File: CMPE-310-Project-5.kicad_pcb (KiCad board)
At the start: 4 copper layers, 10 parts, among them J1 DSUB-9, U1 max235cpg, U2 8255, U3 pkd8279, U4 8086_Min_Mode, U5 8255, U6 8255

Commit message: File Updates (RAM wired)
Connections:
- Bank0 pad 10: unconnected-(Bank0-Pad10) -> /CMOS_wires/A3
- Bank0 pad 11: unconnected-(Bank0-Pad11) -> /CMOS_wires/A2
- Bank0 pad 12: unconnected-(Bank0-Pad12) -> /CMOS_wires/A1
- Bank0 pad 2: unconnected-(Bank0-Pad2) -> /CMOS_wires/A17
- Bank0 pad 22: unconnected-(Bank0-Pad22) -> /CMOS_wires/CS1
- Bank0 pad 23: unconnected-(Bank0-Pad23) -> /CMOS_wires/A11
- Bank0 pad 24: unconnected-(Bank0-Pad24) -> /RD
- Bank0 pad 25: unconnected-(Bank0-Pad25) -> /CMOS_wires/A12
- Bank0 pad 26: unconnected-(Bank0-Pad26) -> /CMOS_wires/A10
- Bank0 pad 27: unconnected-(Bank0-Pad27) -> /CMOS_wires/A9
- Bank0 pad 28: unconnected-(Bank0-Pad28) -> /CMOS_wires/A14
- Bank0 pad 29: unconnected-(Bank0-Pad29) -> /CMOS_wires/A15
- Bank0 pad 3: unconnected-(Bank0-Pad3) -> /CMOS_wires/A16
- Bank0 pad 31: unconnected-(Bank0-Pad31) -> /WR
- Bank0 pad 4: unconnected-(Bank0-Pad4) -> /CMOS_wires/A13
- Bank0 pad 5: unconnected-(Bank0-Pad5) -> /CMOS_wires/A8
- Bank0 pad 6: unconnected-(Bank0-Pad6) -> /CMOS_wires/A7
- Bank0 pad 7: unconnected-(Bank0-Pad7) -> /CMOS_wires/A6
- Bank0 pad 8: unconnected-(Bank0-Pad8) -> /CMOS_wires/A5
- Bank0 pad 9: unconnected-(Bank0-Pad9) -> /CMOS_wires/A4
- Bank1 pad 10: unconnected-(Bank1-Pad10) -> /CMOS_wires/A3
- Bank1 pad 11: unconnected-(Bank1-Pad11) -> /CMOS_wires/A2
- Bank1 pad 12: unconnected-(Bank1-Pad12) -> /CMOS_wires/A1
- Bank1 pad 2: unconnected-(Bank1-Pad2) -> /CMOS_wires/A17
- Bank1 pad 22: unconnected-(Bank1-Pad22) -> /CMOS_wires/CS1
- Bank1 pad 23: unconnected-(Bank1-Pad23) -> /CMOS_wires/A11
- Bank1 pad 24: unconnected-(Bank1-Pad24) -> /RD
- Bank1 pad 25: unconnected-(Bank1-Pad25) -> /CMOS_wires/A12
- Bank1 pad 26: unconnected-(Bank1-Pad26) -> /CMOS_wires/A9
- Bank1 pad 27: unconnected-(Bank1-Pad27) -> /CMOS_wires/A9
- Bank1 pad 28: unconnected-(Bank1-Pad28) -> /CMOS_wires/A14
- Bank1 pad 29: unconnected-(Bank1-Pad29) -> /CMOS_wires/A15
- Bank1 pad 3: unconnected-(Bank1-Pad3) -> /CMOS_wires/A16
- Bank1 pad 31: unconnected-(Bank1-Pad31) -> /WR
- Bank1 pad 4: unconnected-(Bank1-Pad4) -> /CMOS_wires/A13
- Bank1 pad 5: unconnected-(Bank1-Pad5) -> /CMOS_wires/A8
- Bank1 pad 6: unconnected-(Bank1-Pad6) -> /CMOS_wires/A7
- Bank1 pad 7: unconnected-(Bank1-Pad7) -> /CMOS_wires/A6
- Bank1 pad 8: unconnected-(Bank1-Pad8) -> /CMOS_wires/A5
- Bank1 pad 9: unconnected-(Bank1-Pad9) -> /CMOS_wires/A4

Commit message: Updated PCB
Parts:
- added C1: C, Capacitor_SMD:CP_Elec_3x5.3, F.Cu at (236.0, 243.5)
- added C2: C, Capacitor_SMD:CP_Elec_3x5.3, F.Cu at (226.2, 76.1)
- added D1: DIODE, Diode_SMD:D_0201_0603Metric, F.Cu at (263.3, 209.8)
- added D10: LED, LED_SMD:LED_0201_0603Metric, F.Cu at (-1.19, 106.8)
- added D2: DIODE, Diode_SMD:D_0201_0603Metric, F.Cu at (242.7, 72.1)
- added D3: LED, LED_SMD:LED_0201_0603Metric, F.Cu at (1.49, 108.6)
- added D4: LED, LED_SMD:LED_0201_0603Metric, F.Cu at (-3.87, 106.8)
- added D5: LED, LED_SMD:LED_0201_0603Metric, F.Cu at (-3.87, 108.6)
- added D6: LED, LED_SMD:LED_0201_0603Metric, F.Cu at (-6.55, 106.8)
- added D7: LED, LED_SMD:LED_0201_0603Metric, F.Cu at (-6.55, 108.6)
- added D8: LED, LED_SMD:LED_0201_0603Metric, F.Cu at (1.49, 106.8)
- added D9: LED, LED_SMD:LED_0201_0603Metric, F.Cu at (-1.19, 108.6)
- added J10: Conn_01x04_Male, Connector_Harwin:Harwin_M20-89008xx_1x08_P2.54mm_Horizontal, F.Cu at (315.1, 30.0)
- added J11: Conn_01x03_Male, Connector_Harwin:Harwin_M20-89008xx_1x08_P2.54mm_Horizontal, F.Cu at (304.3, 57.0)
- added J12: Conn_01x03_Male, Connector_Harwin:Harwin_M20-89008xx_1x08_P2.54mm_Horizontal, F.Cu at (330.7, 30.0)
- added J13: Conn_01x02_Male, Connector_Harwin:Harwin_M20-89008xx_1x08_P2.54mm_Horizontal, F.Cu at (285.9, 62.1)
- added J14: DSUB-9, parts:DSUB-9, F.Cu at (249.0, 130.6)
- added J15: Conn_01x03_Male, Connector:FanPinHeader_1x03_P2.54mm_Vertical, F.Cu at (369.2, 49.4)
- added J16: Conn_01x20_Male, Connector:FanPinHeader_1x03_P2.54mm_Vertical, F.Cu at (359.6, 49.4)
- added J17: Conn_01x16_Male, Connector:FanPinHeader_1x03_P2.54mm_Vertical, F.Cu at (348.7, 76.4)
- added J2: Conn_01x08_Male, Connector_Harwin:Harwin_M20-89008xx_1x08_P2.54mm_Horizontal, F.Cu at (81.5, 183.6)
- added J3: Conn_01x08_Male, Connector_Harwin:Harwin_M20-89008xx_1x08_P2.54mm_Horizontal, F.Cu at (55.0, 205.9)
- added J4: Conn_01x08_Male, Connector_Harwin:Harwin_M20-89008xx_1x08_P2.54mm_Horizontal, F.Cu at (97.1, 161.2)
- added J5: Conn_01x08_Male, Connector_Harwin:Harwin_M20-89008xx_1x08_P2.54mm_Horizontal, F.Cu at (81.5, 161.2)
- added J6: Conn_01x08_Male, Connector_Harwin:Harwin_M20-89008xx_1x08_P2.54mm_Horizontal, F.Cu at (70.6, 205.9)
- added J7: Conn_01x08_Male, Connector_Harwin:Harwin_M20-89008xx_1x08_P2.54mm_Horizontal, F.Cu at (86.2, 205.9)
- added J8: Conn_01x08_Male, Connector_Harwin:Harwin_M20-89008xx_1x08_P2.54mm_Horizontal, F.Cu at (65.8, 161.2)
- added J9: Conn_01x08_Male, Connector_Harwin:Harwin_M20-89008xx_1x08_P2.54mm_Horizontal, F.Cu at (97.1, 183.6)
- added R1: R, Resistor_SMD:R_0201_0603Metric, F.Cu at (283.3, 205.7)
- added R2: 10k, Resistor_SMD:R_0201_0603Metric, F.Cu at (252.2, 214.0)
- added R3: R, Resistor_SMD:R_0201_0603Metric, F.Cu at (230.8, 74.6)
- added SW1: SW_Push, Button_Switch_Keyboard:SW_Cherry_MX_1.00u_PCB, F.Cu at (274.5, 193.7)
- added SW10: SW_Push, Button_Switch_Keyboard:SW_Cherry_MX_1.00u_PCB, F.Cu at (128.7, 23.9)
- added SW11: SW_Push, Button_Switch_Keyboard:SW_Cherry_MX_1.00u_PCB, F.Cu at (148.9, 23.9)
- added SW12: SW_Push, Button_Switch_Keyboard:SW_Cherry_MX_1.00u_PCB, F.Cu at (96.3, 120.9)
- added SW13: SW_Push, Button_Switch_Keyboard:SW_Cherry_MX_1.00u_PCB, F.Cu at (189.3, 23.9)
- added SW14: SW_Push, Button_Switch_Keyboard:SW_Cherry_MX_1.00u_PCB, F.Cu at (15.5, 131.3)
- added SW15: SW_Push, Button_Switch_Keyboard:SW_Cherry_MX_1.00u_PCB, F.Cu at (55.9, 124.5)
- added SW16: SW_Push, Button_Switch_Keyboard:SW_Cherry_MX_1.00u_PCB, F.Cu at (79.9, 84.0)
- added SW17: SW_Push, Button_Switch_Keyboard:SW_Cherry_MX_1.00u_PCB, F.Cu at (117.9, 91.2)
- added SW18: SW_Push, Button_Switch_Keyboard:SW_Cherry_MX_1.00u_PCB, F.Cu at (169.1, 23.9)
- added SW19: SW_Push, Button_Switch_Keyboard:SW_Cherry_MX_1.00u_PCB, F.Cu at (68.2, 104.2)
- added SW2: SW_Push, Button_Switch_Keyboard:SW_Cherry_MX_1.00u_PCB, F.Cu at (324.7, 46.2)
- added SW20: SW_Push, Button_Switch_Keyboard:SW_Cherry_MX_1.00u_PCB, F.Cu at (138.1, 84.5)
- added SW21: SW_Push, Button_Switch_Keyboard:SW_Cherry_MX_1.00u_PCB, F.Cu at (178.5, 44.0)
- added SW22: SW_Push, Button_Switch_Keyboard:SW_Cherry_MX_1.00u_PCB, F.Cu at (117.9, 111.5)
- added SW23: SW_Push, Button_Switch_Keyboard:SW_Cherry_MX_1.00u_PCB, F.Cu at (138.1, 44.0)
- added SW24: SW_Push, Button_Switch_Keyboard:SW_Cherry_MX_1.00u_PCB, F.Cu at (138.1, 64.2)
- added SW25: SW_Push, Button_Switch_Keyboard:SW_Cherry_MX_1.00u_PCB, F.Cu at (117.9, 71.0)
- added SW26: SW_Push, Button_Switch_Keyboard:SW_Cherry_MX_1.00u_PCB, F.Cu at (48.0, 104.3)
- added SW27: SW_Push, Button_Switch_Keyboard:SW_Cherry_MX_1.00u_PCB, F.Cu at (76.1, 124.3)
- added SW28: SW_DIP_x08, Connector_DIN:DIN41612_D_2x8_Female_Vertical_THT, F.Cu at (96.4, 28.0)
- added SW3: SW_Push, Button_Switch_Keyboard:SW_Cherry_MX_1.00u_PCB, F.Cu at (158.3, 44.0)
- added SW4: SW_Push, Button_Switch_Keyboard:SW_Cherry_MX_1.00u_PCB, F.Cu at (158.3, 64.2)
- added SW5: SW_Push, Button_Switch_Keyboard:SW_Cherry_MX_1.00u_PCB, F.Cu at (27.1, 111.0)
- added SW6: SW_Push, Button_Switch_Keyboard:SW_Cherry_MX_1.00u_PCB, F.Cu at (59.7, 84.0)
- added SW7: SW_Push, Button_Switch_Keyboard:SW_Cherry_MX_1.00u_PCB, F.Cu at (116.5, 131.7)
- added SW8: SW_Push, Button_Switch_Keyboard:SW_Cherry_MX_1.00u_PCB, F.Cu at (35.7, 131.2)
- added SW9: SW_Push, Button_Switch_Keyboard:SW_Cherry_MX_1.00u_PCB, F.Cu at (117.9, 50.9)
- added U10: 74LVC1G332, Package_TO_SOT_SMD:SOT-23-6, F.Cu at (183.4, 189.4)
- added U11: 74LS138, Package_DIP:DIP-16_W7.62mm, F.Cu at (160.7, 189.2)
- added U12: CY7C199, Package_DIP:DIP-28_W7.62mm, F.Cu at (193.3, 152.1)
- added U13: PAL16L8, Package_DIP:DIP-20_W7.62mm, F.Cu at (261.3, 58.1)
- added U14: 16550, Package_DIP:DIP-40_W15.24mm, F.Cu at (242.8, 20.9)
- added U15: CY7C199, Package_DIP:DIP-28_W7.62mm, F.Cu at (160.7, 152.1)
- added U16: 4012, Package_DIP:DIP-12_W7.62mm, F.Cu at (204.1, 152.1)
- added U17: CY7C199, Package_DIP:DIP-28_W7.62mm, F.Cu at (182.4, 152.1)
- added U18: 8259A, Package_DIP:DIP-28_W15.24mm, F.Cu at (261.2, 20.9)
- added U19: PAL16L8, Package_DIP:DIP-20_W7.62mm, F.Cu at (298.1, 20.9)
- added U20: pkd8279, parts:pkd8279, F.Cu at (239.7, 70.4)
- added U21: 8254, Package_DIP:DIP-24_W15.24mm, F.Cu at (279.6, 20.9)
- added U22: max235cpg, parts:max235cpg, F.Cu at (249.3, 120.6)
- added U23: 74LS244, Package_DIP:DIP-20_W7.62mm, F.Cu at (391.5, 20.9)
- added U24: 74LS373, Package_DIP:DIP-20_W7.62mm, F.Cu at (348.1, 20.9)
- added U25: 74LS373, Package_DIP:DIP-20_W7.62mm, F.Cu at (369.8, 20.9)
- added U26: 74LS373, Package_DIP:DIP-20_W7.62mm, F.Cu at (348.1, 47.9)
- added U27: 74LS245, Package_DIP:DIP-20_W7.62mm, F.Cu at (380.6, 20.9)
- added U28: 74LS245, Package_DIP:DIP-20_W7.62mm, F.Cu at (358.9, 20.9)
- added U29: 74LS30, Package_DIP:PowerIntegrations_eDIP-12B, F.Cu at (87.4, 100.7)
- added U30: 74LS138, Package_DIP:DIP-16_W7.62mm, F.Cu at (26.2, 81.0)
- added U31: 74LS04, Package_DIP:DIP-14_W7.62mm, F.Cu at (167.5, 61.3)
- added U32: 74LS244, Package_DIP:DIP-20_W7.62mm, F.Cu at (-6.38, 118.0)
- added U33: PAL16L8, Package_DIP:DIP-20_W7.62mm, F.Cu at (4.46, 81.0)
- added U34: 74LS374, Package_DIP:DIP-20_W7.62mm, F.Cu at (15.3, 81.0)
- added U35: 74LS374, Package_DIP:DIP-20_W7.62mm, F.Cu at (106.9, 20.9)
- added U36: 74LS374, Package_DIP:DIP-20_W7.62mm, F.Cu at (-6.38, 81.0)
- added U37: MAN71A, Display_7Segment:MAN71A, F.Cu at (4.99, 108.5)
- added U38: MAN71A, Display_7Segment:MAN71A, F.Cu at (37.5, 81.5)
- added U39: 74LS04, Package_DIP:DIP-14_W7.62mm, F.Cu at (123.9, 195.6)
- added U40: 4012, Package_DIP:DIP-12_W7.62mm, F.Cu at (145.6, 195.6)
- added U41: 74LS04, Package_DIP:DIP-14_W7.62mm, F.Cu at (187.7, 41.1)
- added U7: PAL16L8, Package_DIP:DIP-20_W7.62mm, F.Cu at (48.8, 152.1)
- added U8: 74LS138, Package_DIP:DIP-16_W7.62mm, F.Cu at (171.6, 189.2)
- added U9: CY7C199, Package_DIP:DIP-28_W7.62mm, F.Cu at (171.6, 152.1)
- added Y1: Crystal, Crystal:Crystal_AT310_D3.0mm_L10.0mm_Horizontal, F.Cu at (283.6, 190.0)
- J1: value DSUB-9 -> Conn_01x08_Male; footprint parts:DSUB-9 -> Connector_Harwin:Harwin_M20-89008xx_1x08_P2.54mm_Horizontal
- U1: value max235cpg -> 8284; footprint parts:max235cpg -> Package_DIP:DIP-18_W7.62mm
- U3: value pkd8279 -> 74LS04; footprint parts:pkd8279 -> Package_DIP:DIP-14_W7.62mm
- moved J1 185.6 mm to (65.8, 183.6)
- moved U4 161.3 mm to (234.2, 190.8)
- moved Bank0 142.0 mm to (123.9, 152.7)
- moved U3 128.4 mm to (134.7, 195.6)
- moved Bank1 121.4 mm to (142.3, 152.7)
- moved U2 90.4 mm to (-6.43, 152.1)
- moved U5 90.4 mm to (30.4, 152.1)
- moved U6 90.4 mm to (12.0, 152.1)
- moved U1 79.2 mm to (252.6, 190.8)
- moved DS1 74.0 mm to (3.54, 22.9)
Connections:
- net /CMOS_wires/CS1 renamed /CMOS_wires/CS
- Bank0 pad 13: unconnected-(Bank0-Pad13) -> /CMOS_wires/D0
- Bank0 pad 14: unconnected-(Bank0-Pad14) -> /CMOS_wires/D1
- Bank0 pad 15: unconnected-(Bank0-Pad15) -> /CMOS_wires/D2
- Bank0 pad 16: unconnected-(Bank0-Pad16) -> GND
- Bank0 pad 17: unconnected-(Bank0-Pad17) -> /CMOS_wires/D3
- Bank0 pad 18: unconnected-(Bank0-Pad18) -> /CMOS_wires/D4
- Bank0 pad 19: unconnected-(Bank0-Pad19) -> /CMOS_wires/D5
- Bank0 pad 20: unconnected-(Bank0-Pad20) -> /CMOS_wires/D6
- Bank0 pad 21: unconnected-(Bank0-Pad21) -> /CMOS_wires/D7
- Bank0 pad 24: /RD -> /CMOS_wires/RD
- Bank0 pad 31: /WR -> /CMOS_wires/WR
- Bank0 pad 32: unconnected-(Bank0-Pad32) -> +5V
- Bank1 pad 13: unconnected-(Bank1-Pad13) -> /CMOS_wires/D0
- Bank1 pad 14: unconnected-(Bank1-Pad14) -> /CMOS_wires/D1
- Bank1 pad 15: unconnected-(Bank1-Pad15) -> /CMOS_wires/D2
- Bank1 pad 16: unconnected-(Bank1-Pad16) -> GND
- Bank1 pad 17: unconnected-(Bank1-Pad17) -> /CMOS_wires/D3
- Bank1 pad 18: unconnected-(Bank1-Pad18) -> /CMOS_wires/D4
- Bank1 pad 19: unconnected-(Bank1-Pad19) -> /CMOS_wires/D5
- Bank1 pad 20: unconnected-(Bank1-Pad20) -> /CMOS_wires/D6
- Bank1 pad 21: unconnected-(Bank1-Pad21) -> /CMOS_wires/D7
- Bank1 pad 24: /RD -> /CMOS_wires/RD
- Bank1 pad 31: /WR -> /CMOS_wires/WR
- Bank1 pad 32: unconnected-(Bank1-Pad32) -> +5V
- DS1 pad 1: unconnected-(DS1-Pad1) -> GND
- DS1 pad 10: unconnected-(DS1-Pad10) -> /INTR_wires/IO_Component_Wires/D3
- DS1 pad 11: unconnected-(DS1-Pad11) -> /INTR_wires/IO_Component_Wires/D4
- DS1 pad 12: unconnected-(DS1-Pad12) -> /INTR_wires/IO_Component_Wires/D5
- DS1 pad 13: unconnected-(DS1-Pad13) -> /INTR_wires/IO_Component_Wires/D6
- DS1 pad 14: unconnected-(DS1-Pad14) -> /INTR_wires/IO_Component_Wires/D7
- DS1 pad 2: unconnected-(DS1-Pad2) -> +5V
- DS1 pad 4: unconnected-(DS1-Pad4) -> /INTR_wires/IO_Component_Wires/A1
- DS1 pad 5: unconnected-(DS1-Pad5) -> Net-(DS1-Pad5)
- DS1 pad 6: unconnected-(DS1-Pad6) -> Net-(DS1-Pad6)
- DS1 pad 7: unconnected-(DS1-Pad7) -> /INTR_wires/IO_Component_Wires/D0
- DS1 pad 8: unconnected-(DS1-Pad8) -> /INTR_wires/IO_Component_Wires/D1
- DS1 pad 9: unconnected-(DS1-Pad9) -> /INTR_wires/IO_Component_Wires/D2
- J1 pad 1: unconnected-(J1-Pad1) -> Net-(J1-Pad1)
- J1 pad 2: unconnected-(J1-Pad2) -> Net-(J1-Pad2)
- J1 pad 3: unconnected-(J1-Pad3) -> Net-(J1-Pad3)
- J1 pad 4: unconnected-(J1-Pad4) -> Net-(J1-Pad4)
- J1 pad 5: unconnected-(J1-Pad5) -> Net-(J1-Pad5)
- J1 pad 6: unconnected-(J1-Pad6) -> Net-(J1-Pad6)
- J1 pad 7: unconnected-(J1-Pad7) -> Net-(J1-Pad7)
- J1 pad 8: unconnected-(J1-Pad8) -> Net-(J1-Pad8)
- U1 pad 1: unconnected-(U1-Pad1) -> GND
- U1 pad 10: unconnected-(U1-Pad10) -> /8255_wires/RESET
- U1 pad 11: unconnected-(U1-Pad11) -> Net-(C1-Pad1)
- U1 pad 13: unconnected-(U1-Pad13) -> GND
- U1 pad 16: unconnected-(U1-Pad16) -> Net-(U1-Pad16)
- U1 pad 17: unconnected-(U1-Pad17) -> Net-(U1-Pad17)
- U1 pad 18: unconnected-(U1-Pad18) -> +5V
- U1 pad 2: unconnected-(U1-Pad2) -> /INTR_wires/PCLK
- U1 pad 8: unconnected-(U1-Pad8) -> Net-(U1-Pad8)
- U2 pad 1: unconnected-(U2-Pad1) -> Net-(J1-Pad5)
- U2 pad 10: unconnected-(U2-Pad10) -> Net-(J3-Pad1)
- U2 pad 11: unconnected-(U2-Pad11) -> Net-(J3-Pad2)
- U2 pad 12: unconnected-(U2-Pad12) -> Net-(J3-Pad3)
- U2 pad 13: unconnected-(U2-Pad13) -> Net-(J3-Pad4)
- U2 pad 14: unconnected-(U2-Pad14) -> Net-(J3-Pad8)
- U2 pad 15: unconnected-(U2-Pad15) -> Net-(J3-Pad7)
- U2 pad 16: unconnected-(U2-Pad16) -> Net-(J3-Pad6)
- U2 pad 17: unconnected-(U2-Pad17) -> Net-(J3-Pad5)
- U2 pad 18: unconnected-(U2-Pad18) -> Net-(J2-Pad8)
- U2 pad 19: unconnected-(U2-Pad19) -> Net-(J2-Pad7)
- U2 pad 2: unconnected-(U2-Pad2) -> Net-(J1-Pad6)
- U2 pad 20: unconnected-(U2-Pad20) -> Net-(J2-Pad6)
- U2 pad 21: unconnected-(U2-Pad21) -> Net-(J2-Pad5)
- U2 pad 22: unconnected-(U2-Pad22) -> Net-(J2-Pad4)
- U2 pad 23: unconnected-(U2-Pad23) -> Net-(J2-Pad3)
- U2 pad 24: unconnected-(U2-Pad24) -> Net-(J2-Pad2)
- U2 pad 25: unconnected-(U2-Pad25) -> Net-(J2-Pad1)
- U2 pad 26: unconnected-(U2-Pad26) -> +5V
- U2 pad 27: unconnected-(U2-Pad27) -> /8255_wires/D7
- U2 pad 28: unconnected-(U2-Pad28) -> /8255_wires/D6
- U2 pad 29: unconnected-(U2-Pad29) -> /8255_wires/D5
- U2 pad 3: unconnected-(U2-Pad3) -> Net-(J1-Pad7)
- U2 pad 30: unconnected-(U2-Pad30) -> /8255_wires/D4
- U2 pad 31: unconnected-(U2-Pad31) -> /8255_wires/D3
- U2 pad 32: unconnected-(U2-Pad32) -> /8255_wires/D2
- U2 pad 33: unconnected-(U2-Pad33) -> /8255_wires/D1
- U2 pad 34: unconnected-(U2-Pad34) -> /8255_wires/D0
- U2 pad 35: unconnected-(U2-Pad35) -> /8255_wires/RESET
- U2 pad 36: unconnected-(U2-Pad36) -> /8255_wires/WR
- U2 pad 37: unconnected-(U2-Pad37) -> Net-(J1-Pad1)
- U2 pad 38: unconnected-(U2-Pad38) -> Net-(J1-Pad2)
- U2 pad 39: unconnected-(U2-Pad39) -> Net-(J1-Pad3)
- U2 pad 4: unconnected-(U2-Pad4) -> Net-(J1-Pad8)
- U2 pad 40: unconnected-(U2-Pad40) -> Net-(J1-Pad4)
- U2 pad 5: unconnected-(U2-Pad5) -> /8255_wires/RD
- U2 pad 6: unconnected-(U2-Pad6) -> Net-(U2-Pad6)
- U2 pad 7: unconnected-(U2-Pad7) -> GND
- U3 pad 1: unconnected-(U3-Pad1) -> /CMOS_wires/A0
- U3 pad 10: unconnected-(U3-Pad10) -> (no net)
- U3 pad 11: unconnected-(U3-Pad11) -> (no net)
- U3 pad 12: unconnected-(U3-Pad12) -> (no net)
- U3 pad 13: unconnected-(U3-Pad13) -> (no net)
- U3 pad 14: unconnected-(U3-Pad14) -> (no net)
- U3 pad 2: unconnected-(U3-Pad2) -> Net-(U16-Pad12)
- U3 pad 3: unconnected-(U3-Pad3) -> /CMOS_wires/A0
- U3 pad 4: unconnected-(U3-Pad4) -> /CMOS_wires/A0
- U3 pad 5: unconnected-(U3-Pad5) -> (no net)
- U3 pad 6: unconnected-(U3-Pad6) -> (no net)
- U3 pad 7: unconnected-(U3-Pad7) -> (no net)
- U3 pad 8: unconnected-(U3-Pad8) -> (no net)
- U3 pad 9: unconnected-(U3-Pad9) -> (no net)
- U4 pad 1: unconnected-(U4-Pad1) -> GND
- U4 pad 10: /A6 -> /Bus_wires/AD6
- U4 pad 11: /A5 -> /Bus_wires/AD5
- U4 pad 12: /A4 -> /Bus_wires/AD4
- U4 pad 13: /A3 -> /Bus_wires/AD3
- U4 pad 14: /A2 -> /Bus_wires/AD2
- U4 pad 15: /A1 -> /Bus_wires/AD1
- U4 pad 16: /A0 -> /CMOS_wires/A0
- U4 pad 17: unconnected-(U4-Pad17) -> /INTR_wires/NMI
- U4 pad 18: unconnected-(U4-Pad18) -> /INTR_wires/INTR
- U4 pad 19: unconnected-(U4-Pad19) -> Net-(U1-Pad8)
- U4 pad 2: /A14 -> /Bus_wires/AD14
- U4 pad 20: unconnected-(U4-Pad20) -> GND
- U4 pad 21: unconnected-(U4-Pad21) -> /8255_wires/RESET
- U4 pad 24: unconnected-(U4-Pad24) -> /INTR_wires/INTA
- U4 pad 25: unconnected-(U4-Pad25) -> /Bus_wires/ALE
- U4 pad 26: unconnected-(U4-Pad26) -> /Bus_wires/DEN
- U4 pad 27: unconnected-(U4-Pad27) -> /Bus_wires/DT/R
- U4 pad 28: /M/IO -> /MRDC
- U4 pad 29: /WR -> /Bus_wires/WR
- U4 pad 3: /A13 -> /Bus_wires/AD13
- U4 pad 32: /RD -> /Bus_wires/RD
- U4 pad 33: unconnected-(U4-Pad33) -> Net-(R2-Pad2)
- U4 pad 34: unconnected-(U4-Pad34) -> /Bus_wires/BHE/S7
- U4 pad 35: /A19 -> /CMOS_wires/A19
- U4 pad 36: /A18 -> /CMOS_wires/A18
- U4 pad 37: /A17 -> /Bus_wires/A17/S4
- U4 pad 38: /A16 -> /Bus_wires/A16/S3
- U4 pad 39: /A15 -> /Bus_wires/AD15
- U4 pad 4: /A12 -> /Bus_wires/AD12
- U4 pad 40: unconnected-(U4-Pad40) -> +5V
- U4 pad 5: /A11 -> /Bus_wires/AD11
- U4 pad 6: /A10 -> /Bus_wires/AD10
- U4 pad 7: /A9 -> /Bus_wires/AD9
- U4 pad 8: /A8 -> /Bus_wires/AD8
- U4 pad 9: /A7 -> /Bus_wires/AD7
- U5 pad 1: unconnected-(U5-Pad1) -> Net-(J4-Pad5)
- U5 pad 10: unconnected-(U5-Pad10) -> Net-(J6-Pad1)
- U5 pad 11: unconnected-(U5-Pad11) -> Net-(J6-Pad2)
- U5 pad 12: unconnected-(U5-Pad12) -> Net-(J6-Pad3)
- U5 pad 13: unconnected-(U5-Pad13) -> Net-(J6-Pad4)
- U5 pad 14: unconnected-(U5-Pad14) -> Net-(J6-Pad8)
- U5 pad 15: unconnected-(U5-Pad15) -> Net-(J6-Pad7)
- U5 pad 16: unconnected-(U5-Pad16) -> Net-(J6-Pad6)
- U5 pad 17: unconnected-(U5-Pad17) -> Net-(J6-Pad5)
- U5 pad 18: unconnected-(U5-Pad18) -> Net-(J5-Pad8)
- U5 pad 19: unconnected-(U5-Pad19) -> Net-(J5-Pad7)
- U5 pad 2: unconnected-(U5-Pad2) -> Net-(J4-Pad6)
- U5 pad 20: unconnected-(U5-Pad20) -> Net-(J5-Pad6)
- U5 pad 21: unconnected-(U5-Pad21) -> Net-(J5-Pad5)
- U5 pad 22: unconnected-(U5-Pad22) -> Net-(J5-Pad4)
- U5 pad 23: unconnected-(U5-Pad23) -> Net-(J5-Pad3)
- U5 pad 24: unconnected-(U5-Pad24) -> Net-(J5-Pad2)
- U5 pad 25: unconnected-(U5-Pad25) -> Net-(J5-Pad1)
- U5 pad 26: unconnected-(U5-Pad26) -> +5V
- U5 pad 27: unconnected-(U5-Pad27) -> /8255_wires/D7
- U5 pad 28: unconnected-(U5-Pad28) -> /8255_wires/D6
- U5 pad 29: unconnected-(U5-Pad29) -> /8255_wires/D5
- U5 pad 3: unconnected-(U5-Pad3) -> Net-(J4-Pad7)
- U5 pad 30: unconnected-(U5-Pad30) -> /8255_wires/D4
- U5 pad 31: unconnected-(U5-Pad31) -> /8255_wires/D3
- U5 pad 32: unconnected-(U5-Pad32) -> /8255_wires/D2
- U5 pad 33: unconnected-(U5-Pad33) -> /8255_wires/D1
- U5 pad 34: unconnected-(U5-Pad34) -> /8255_wires/D0
- U5 pad 35: unconnected-(U5-Pad35) -> /8255_wires/RESET
- U5 pad 36: unconnected-(U5-Pad36) -> /8255_wires/WR
- U5 pad 37: unconnected-(U5-Pad37) -> Net-(J4-Pad1)
- U5 pad 38: unconnected-(U5-Pad38) -> Net-(J4-Pad2)
- U5 pad 39: unconnected-(U5-Pad39) -> Net-(J4-Pad3)
- U5 pad 4: unconnected-(U5-Pad4) -> Net-(J4-Pad8)
- U5 pad 40: unconnected-(U5-Pad40) -> Net-(J4-Pad4)
- U5 pad 5: unconnected-(U5-Pad5) -> /8255_wires/RD
- U5 pad 6: unconnected-(U5-Pad6) -> Net-(U5-Pad6)
- U5 pad 7: unconnected-(U5-Pad7) -> GND
- U5 pad 8: unconnected-(U5-Pad8) -> /8255_wires/A2
- U5 pad 9: unconnected-(U5-Pad9) -> /8255_wires/A1
- U6 pad 1: unconnected-(U6-Pad1) -> Net-(J7-Pad5)
- U6 pad 10: unconnected-(U6-Pad10) -> Net-(J9-Pad1)
- U6 pad 11: unconnected-(U6-Pad11) -> Net-(J9-Pad2)
- U6 pad 12: unconnected-(U6-Pad12) -> Net-(J9-Pad3)
- U6 pad 13: unconnected-(U6-Pad13) -> Net-(J9-Pad4)
- U6 pad 14: unconnected-(U6-Pad14) -> Net-(J9-Pad8)
- U6 pad 15: unconnected-(U6-Pad15) -> Net-(J9-Pad7)
- U6 pad 16: unconnected-(U6-Pad16) -> Net-(J9-Pad6)
- U6 pad 17: unconnected-(U6-Pad17) -> Net-(J9-Pad5)
- U6 pad 18: unconnected-(U6-Pad18) -> Net-(J8-Pad8)
- U6 pad 19: unconnected-(U6-Pad19) -> Net-(J8-Pad7)
- U6 pad 2: unconnected-(U6-Pad2) -> Net-(J7-Pad6)
- U6 pad 20: unconnected-(U6-Pad20) -> Net-(J8-Pad6)
- U6 pad 21: unconnected-(U6-Pad21) -> Net-(J8-Pad5)
- U6 pad 22: unconnected-(U6-Pad22) -> Net-(J8-Pad4)
- U6 pad 23: unconnected-(U6-Pad23) -> Net-(J8-Pad3)
- U6 pad 24: unconnected-(U6-Pad24) -> Net-(J8-Pad2)
- U6 pad 25: unconnected-(U6-Pad25) -> Net-(J8-Pad1)
- U6 pad 26: unconnected-(U6-Pad26) -> +5V
- U6 pad 27: unconnected-(U6-Pad27) -> /8255_wires/D7
- U6 pad 28: unconnected-(U6-Pad28) -> /8255_wires/D6
- U6 pad 29: unconnected-(U6-Pad29) -> /8255_wires/D5
- U6 pad 3: unconnected-(U6-Pad3) -> Net-(J7-Pad7)
- U6 pad 30: unconnected-(U6-Pad30) -> /8255_wires/D4
- U6 pad 31: unconnected-(U6-Pad31) -> /8255_wires/D3
- U6 pad 32: unconnected-(U6-Pad32) -> /8255_wires/D2
- U6 pad 33: unconnected-(U6-Pad33) -> /8255_wires/D1
- U6 pad 34: unconnected-(U6-Pad34) -> /8255_wires/D0
- U6 pad 35: unconnected-(U6-Pad35) -> /8255_wires/RESET
- U6 pad 36: unconnected-(U6-Pad36) -> /8255_wires/WR
- U6 pad 37: unconnected-(U6-Pad37) -> Net-(J7-Pad1)
- U6 pad 38: unconnected-(U6-Pad38) -> Net-(J7-Pad2)
- U6 pad 39: unconnected-(U6-Pad39) -> Net-(J7-Pad3)
- U6 pad 4: unconnected-(U6-Pad4) -> Net-(J7-Pad8)
- U6 pad 40: unconnected-(U6-Pad40) -> Net-(J7-Pad4)
- U6 pad 5: unconnected-(U6-Pad5) -> /8255_wires/RD
- U6 pad 6: unconnected-(U6-Pad6) -> Net-(U6-Pad6)
- U6 pad 7: unconnected-(U6-Pad7) -> GND
- U6 pad 8: unconnected-(U6-Pad8) -> /8255_wires/A2
- U6 pad 9: unconnected-(U6-Pad9) -> /8255_wires/A1
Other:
- board outline added: 637.5 x 419.1 mm

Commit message: PCB wiring
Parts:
- U22: moved to B.Cu
- moved SW26 438.6 mm to (442.0, 297.2)
- moved R1 425.0 mm to (-101.6, 25.4)
- moved Y1 424.1 mm to (-88.9, -12.7), turned to 90 degrees
- moved D1 420.2 mm to (-114.3, 25.4)
- moved SW27 416.1 mm to (442.0, 322.6)
- moved U1 408.5 mm to (-101.6, -12.7)
- moved C1 406.1 mm to (-114.3, 38.1)
- moved SW1 395.3 mm to (-88.9, 38.1)
- moved SW14 392.9 mm to (391.2, 246.4)
- moved U23 385.5 mm to (12.7, -50.8)
- moved SW25 381.2 mm to (442.0, 271.8)
- moved SW16 377.3 mm to (391.2, 297.2)
- moved SW19 376.2 mm to (416.6, 246.4)
- moved SW15 366.2 mm to (391.2, 271.8)
- moved SW22 365.8 mm to (416.6, 322.6)
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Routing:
- net Net-(J3-Pad7): track 0.00 -> 174.2 mm
- net Net-(J3-Pad8): track 0.00 -> 172.7 mm
- net Net-(J2-Pad3): track 0.00 -> 93.3 mm
- net Net-(J2-Pad4): track 0.00 -> 87.4 mm
- net Net-(J1-Pad8): track 0.00 -> 85.9 mm
- net Net-(C1-Pad1): track 0.00 -> 79.5 mm
- net Net-(J1-Pad7): track 0.00 -> 79.1 mm
- net Net-(J1-Pad6): track 0.00 -> 73.4 mm
- net Net-(J1-Pad5): track 0.00 -> 67.6 mm
- net Net-(J3-Pad2): track 0.00 -> 51.5 mm
- net Net-(J2-Pad6): track 0.00 -> 49.4 mm
- net Net-(J2-Pad7): track 0.00 -> 44.0 mm
- net Net-(J3-Pad3): track 0.00 -> 43.5 mm
- net Net-(J3-Pad4): track 0.00 -> 40.1 mm
- net Net-(J3-Pad1): track 0.00 -> 40.1 mm
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
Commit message: Wired 8255 in pcb
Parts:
- moved J6 35.9 mm to (-25.4, 342.9)
- moved J9 28.4 mm to (38.1, 342.9)
- moved J7 25.4 mm to (76.2, 266.7)
- moved J8 25.4 mm to (76.2, 292.1)
- moved U6 25.4 mm to (43.2, 268.0)
- moved J4 12.7 mm to (12.7, 266.7)
- moved J5 12.7 mm to (12.7, 292.1)
- moved U5 12.7 mm to (-20.3, 268.0)
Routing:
- net Net-(U6-Pad6): track 0.00 -> 141.9 mm
- net Net-(J6-Pad7): track 0.00 -> 103.9 mm
- net Net-(J9-Pad8): track 0.00 -> 103.3 mm
- net Net-(J9-Pad7): track 0.00 -> 94.2 mm
- net Net-(J6-Pad8): track 0.00 -> 90.4 mm
- net Net-(J4-Pad8): track 0.00 -> 84.2 mm
- net Net-(J4-Pad7): track 0.00 -> 77.4 mm
- net Net-(U5-Pad6): track 0.00 -> 77.3 mm
- net Net-(J7-Pad7): track 0.00 -> 71.8 mm
- net Net-(J9-Pad5): track 0.00 -> 68.5 mm
- net Net-(J6-Pad5): track 0.00 -> 68.5 mm
- net Net-(J4-Pad6): track 0.00 -> 65.7 mm
- net Net-(J7-Pad6): track 0.00 -> 62.1 mm
- net Net-(J4-Pad5): track 0.00 -> 57.4 mm
- net Net-(J9-Pad4): track 0.00 -> 57.1 mm
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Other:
- copper layers 4 -> 6
- board text added: "Conn_01x08_Male"
- board text added: "J4"
- board text added: "J5"
- board text added: "U5"

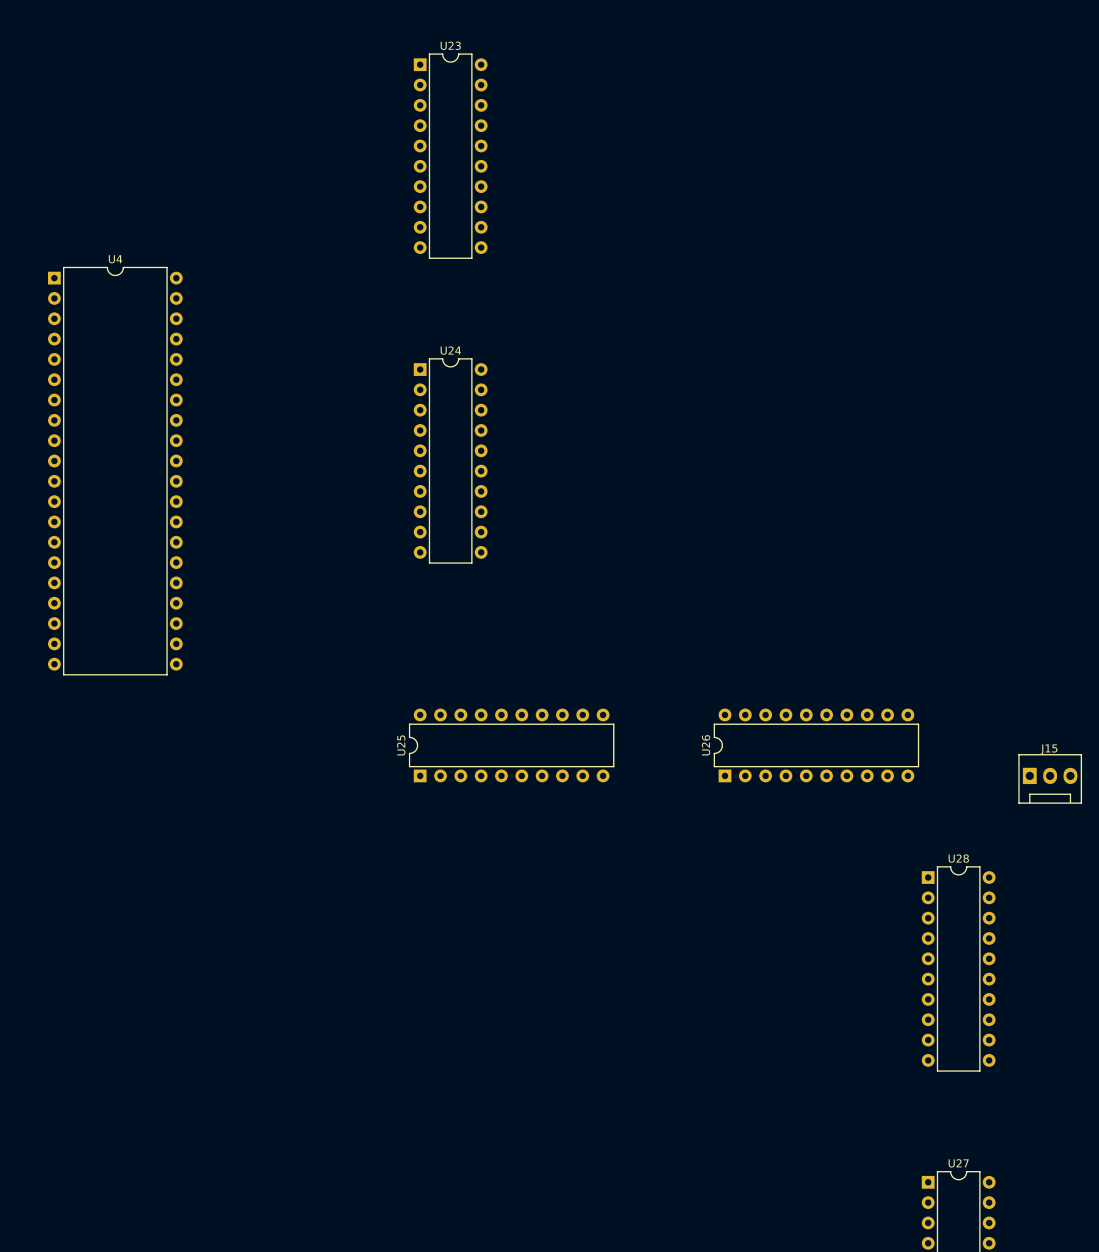
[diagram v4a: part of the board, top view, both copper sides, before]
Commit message: Wired some buses
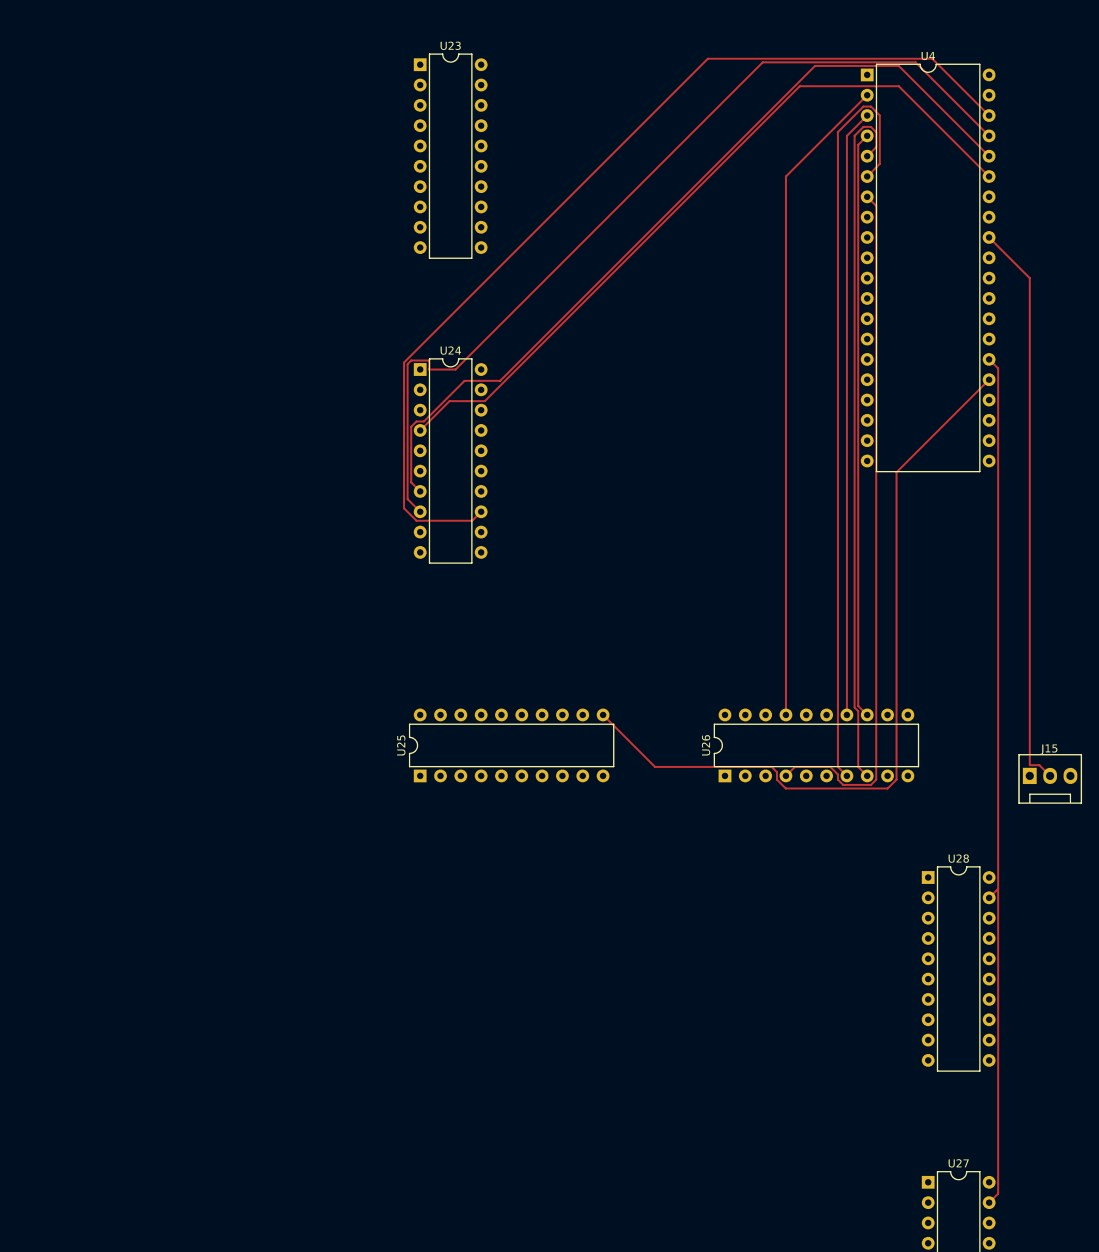
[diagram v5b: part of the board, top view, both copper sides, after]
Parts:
- moved U4 104.7 mm to (68.6, -49.5)
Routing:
- net /Bus_wires/AD12: track 0.00 -> 248.8 mm
- net /Bus_wires/AD14: track 0.00 -> 248.4 mm
- net /Bus_wires/AD13: track 0.00 -> 168.6 mm
- net /Bus_wires/ALE: track 0.00 -> 142.4 mm
- net /Bus_wires/DT/R: track 0.00 -> 122.8 mm
- net /Bus_wires/A16/S3: track 0.00 -> 120.8 mm
- net /Bus_wires/AD7: track 0.00 -> 117.2 mm
- net /Bus_wires/A17/S4: track 0.00 -> 112.8 mm
- net /Bus_wires/AD6: track 0.00 -> 112.5 mm
- net /Bus_wires/DEN: track 0.00 -> 107.9 mm
- net /CMOS_wires/A18: track 0.00 -> 104.1 mm
- net /CMOS_wires/A0: track 0.00 -> 98.5 mm
- net /Bus_wires/AD10: track 0.00 -> 96.2 mm
- net /Bus_wires/AD1: track 0.00 -> 93.9 mm
- net /CMOS_wires/A19: track 0.00 -> 93.6 mm
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
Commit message: pcb wiring
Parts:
- added R4: R, OptoDevice:R_LDR_4.9x4.2mm_P2.54mm_Vertical, F.Cu at (215.9, 304.8)
- added RN1: R_Pack08, Package_DIP:DIP-16_W7.62mm, F.Cu at (204.7, 304.0)
- added RN2: R_Pack08, Package_DIP:DIP-16_W7.62mm, F.Cu at (193.8, 304.0)
- J16: footprint Connector:FanPinHeader_1x03_P2.54mm_Vertical -> Connector_Harwin:Harwin_M20-89020xx_1x20_P2.54mm_Horizontal
- J17: footprint Connector:FanPinHeader_1x03_P2.54mm_Vertical -> Connector_Harwin:Harwin_M20-89016xx_1x16_P2.54mm_Horizontal
- U16: footprint Package_DIP:DIP-12_W7.62mm -> Package_DIP:DIP-14_W7.62mm
- moved J17 45.8 mm to (139.7, 76.2)
- moved J16 40.2 mm to (114.3, 0.00)
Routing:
- net /Bus_wires/AD15: track 89.0 -> 284.1 mm
- net /Bus_wires/AD13: track 168.6 -> 338.3 mm
- net /Bus_wires/AD12: track 248.8 -> 413.0 mm
- net /Bus_wires/AD11: track 87.6 -> 246.3 mm
- net /Bus_wires/AD10: track 96.2 -> 249.5 mm
- net /Bus_wires/AD9: track 86.6 -> 237.3 mm
- net /Bus_wires/AD8: track 78.4 -> 220.8 mm
- net /Bus_wires/AD7: track 117.2 -> 236.3 mm
- net /Bus_wires/WR: track 72.1 -> 188.8 mm
- net /Bus_wires/DT/R: track 122.8 -> 236.5 mm
- net /Bus_wires/AD6: track 112.5 -> 224.4 mm
- net /MRDC: track 61.4 -> 166.0 mm
- net /Bus_wires/AD4: track 85.8 -> 186.3 mm
- net /Bus_wires/AD5: track 71.4 -> 169.9 mm
- net /Bus_wires/AD3: track 72.9 -> 167.3 mm
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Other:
- copper layers 6 -> 8
